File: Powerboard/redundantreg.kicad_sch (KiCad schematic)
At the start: 24 parts, among them Q10 MCH6351, Q9 MCH6351, U6 LM2679T-3.3-iclr, U7 LM2679T-3.3-iclr, U8 LTC4412xS6, U9 LTC4412xS6

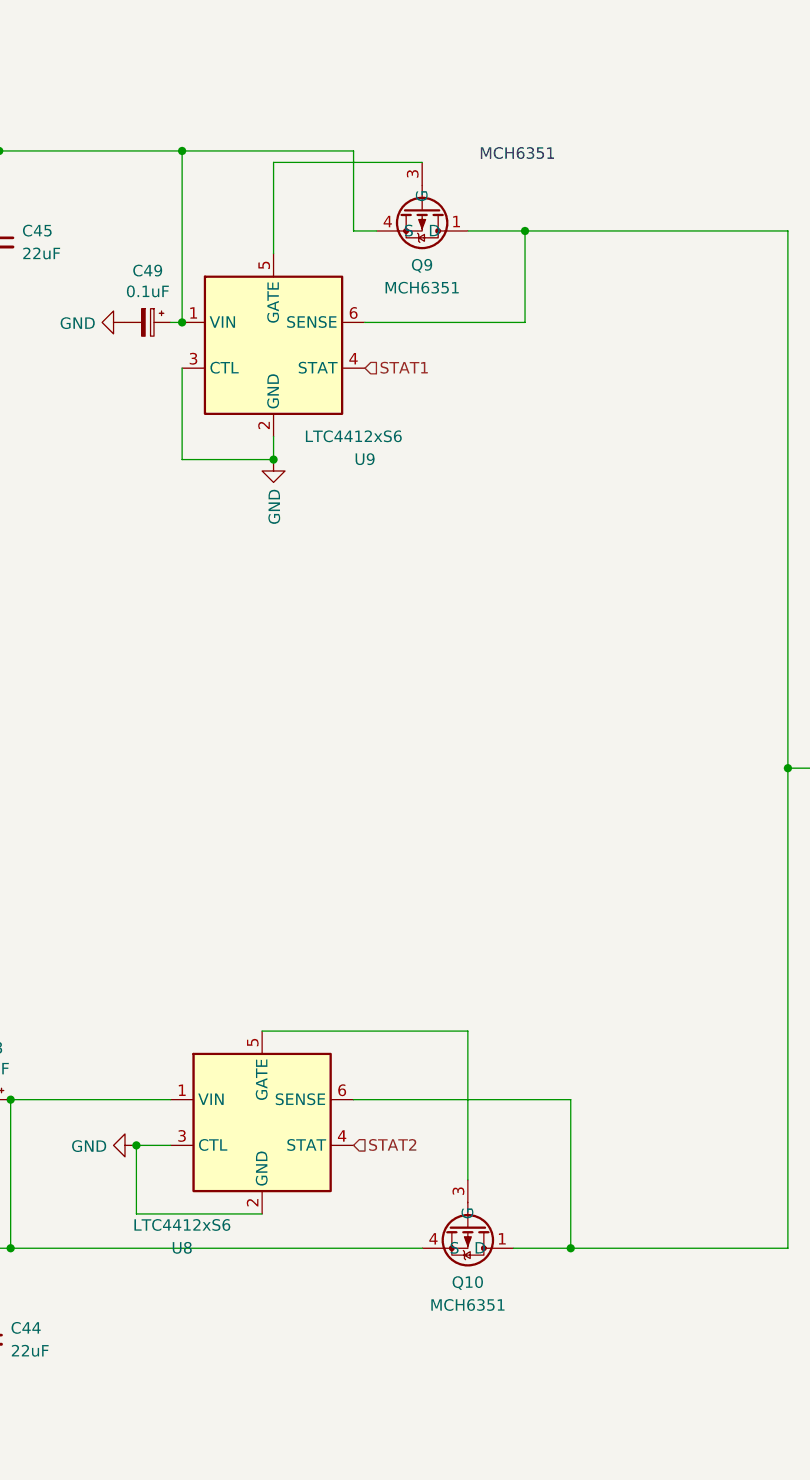
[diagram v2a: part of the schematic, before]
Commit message: swapping mosfets the right way around
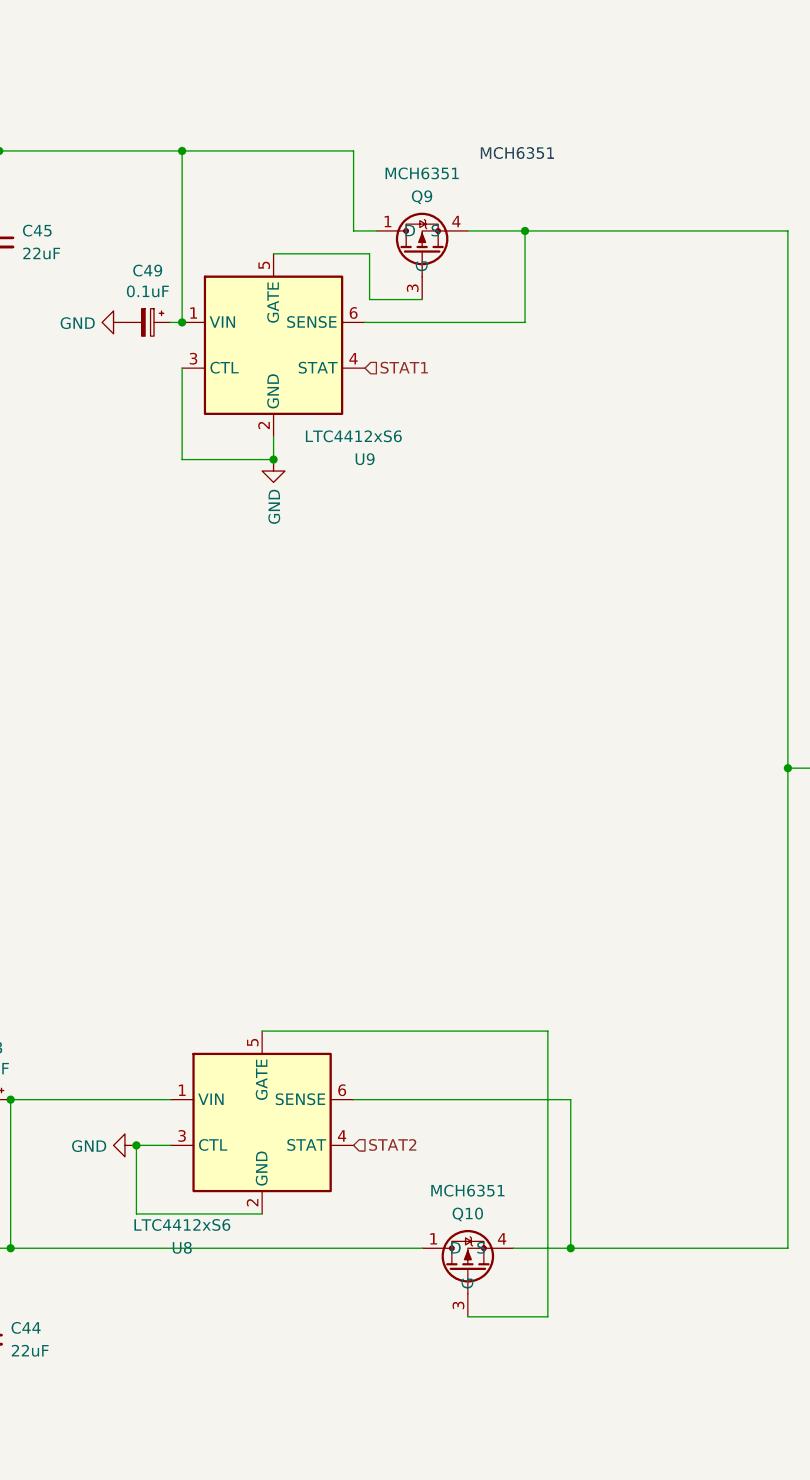
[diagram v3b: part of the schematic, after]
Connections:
- net Vout: now also Q10.4 (S), Q9.4 (S); no longer Q10.1 (D), Q10.2 (D), Q10.5 (D), Q10.6 (D), Q9.1 (D), Q9.2 (D), Q9.5 (D), Q9.6 (D)
- net at C38.1, C40.1, C44.1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: now also Q10.1 (D), Q10.2 (D), Q10.5 (D), Q10.6 (D); no longer Q10.4 (S)
- net at C39.1, C41.1, C45.1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: now also Q9.1 (D), Q9.2 (D), Q9.5 (D), Q9.6 (D); no longer Q9.4 (S)
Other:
- moved on the sheet: Q10, Q9
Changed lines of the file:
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@@
-    (stroke (width 0) (type default) (color 0 0 0 0))
-  )
-  (wire (pts (xy 200.66 26.67) (xy 200.66 36.83))
-    (stroke (width 0) (type default) (color 0 0 0 0))
-  )
-  (wire (pts (xy 200.66 26.67) (xy 217.17 26.67))
     (stroke (width 0) (type default) (color 0 0 0 0))
   )
@@
     (stroke (width 0) (type default) (color 0 0 0 0))
   )
+  (wire (pts (xy 200.66 36.83) (xy 211.328 36.83))
+    (stroke (width 0) (type default) (color 0 0 0 0))
+  )
   (wire (pts (xy 158.75 25.4) (xy 163.83 25.4))
     (stroke (width 0) (type default) (color 0 0 0 0))
@@
     (stroke (width 0) (type default) (color 0 0 0 0))
   )
+  (wire (pts (xy 231.14 154.94) (xy 222.25 154.94))
+    (stroke (width 0) (type default) (color 0 0 0 0))
+  )
   (wire (pts (xy 158.75 147.32) (xy 163.83 147.32))
     (stroke (width 0) (type default) (color 0 0 0 0))
@@
     (stroke (width 0) (type default) (color 0 0 0 0))
   )
-  (wire (pts (xy 222.25 123.19) (xy 222.25 139.7))
-    (stroke (width 0) (type default) (color 0 0 0 0))
-  )
   (wire (pts (xy 190.5 25.4) (xy 190.5 44.45))
     (stroke (width 0) (type default) (color 0 0 0 0))
@@
     (stroke (width 0) (type default) (color 0 0 0 0))
   )
-  (wire (pts (xy 199.39 123.19) (xy 222.25 123.19))
-    (stroke (width 0) (type default) (color 0 0 0 0))
-  )
   (wire (pts (xy 163.83 39.37) (xy 163.83 41.91))
     (stroke (width 0) (type default) (color 0 0 0 0))
@@
     (stroke (width 0) (type default) (color 0 0 0 0))
   )
+  (wire (pts (xy 199.39 123.19) (xy 231.14 123.19))
+    (stroke (width 0) (type default) (color 0 0 0 0))
+  )
   (wire (pts (xy 189.23 44.45) (xy 190.5 44.45))
     (stroke (width 0) (type default) (color 0 0 0 0))
@@
     (stroke (width 0) (type default) (color 0 0 0 0))
   )
+  (wire (pts (xy 231.14 123.19) (xy 231.14 154.94))
+    (stroke (width 0) (type default) (color 0 0 0 0))
+  )
   (wire (pts (xy 190.5 59.69) (xy 200.66 59.69))
     (stroke (width 0) (type default) (color 0 0 0 0))
@@
     (stroke (width 0) (type default) (color 0 0 0 0))
   )
+  (wire (pts (xy 211.328 36.83) (xy 211.328 41.91))
+    (stroke (width 0) (type default) (color 0 0 0 0))
+  )
   (wire (pts (xy 25.4 147.32) (xy 64.77 147.32))
     (stroke (width 0) (type default) (color 0 0 0 0))
@@
   )
   (wire (pts (xy 189.23 135.89) (xy 185.42 135.89))
+    (stroke (width 0) (type default) (color 0 0 0 0))
+  )
+  (wire (pts (xy 211.328 41.91) (xy 217.17 41.91))
     (stroke (width 0) (type default) (color 0 0 0 0))
   )
@@
     (pin "2")
   )
-  (symbol (lib_id "iclr:MCH6351") (at 236.22 22.86 270) (unit 1)
-    (in_bom yes) (on_board yes)
-    (property "Reference" "Q9" (id 0) (at 217.17 38.1 90))
-    (property "Value" "MCH6351" (id 1) (at 217.17 40.64 90))
-    (property "Footprint" "Package_TO_SOT_SMD:SOT-363_SC-70-6" (id 2) (at 218.44 38.1 0)
-      (effects (font (size 1.27 1.27)) hide)
-    )
-    (property "Datasheet" "" (id 3) (at 218.44 38.1 0)
+  (symbol (lib_id "iclr:MCH6351") (at 198.12 45.72 90) (unit 1)
+    (in_bom yes) (on_board yes)
+    (property "Reference" "Q9" (id 0) (at 217.17 30.48 90))
+    (property "Value" "MCH6351" (id 1) (at 217.17 27.94 90))
+    (property "Footprint" "Package_TO_SOT_SMD:SOT-363_SC-70-6" (id 2) (at 215.9 30.48 0)
+      (effects (font (size 1.27 1.27)) hide)
+    )
+    (property "Datasheet" "" (id 3) (at 215.9 30.48 0)
       (effects (font (size 1.27 1.27)) hide)
     )
@@
     (pin "2")
   )
-  (symbol (lib_id "iclr:MCH6351") (at 241.3 135.89 270) (unit 1)
-    (in_bom yes) (on_board yes)
-    (property "Reference" "Q10" (id 0) (at 222.25 151.13 90))
-    (property "Value" "MCH6351" (id 1) (at 222.25 153.67 90))
-    (property "Footprint" "Package_TO_SOT_SMD:SOT-363_SC-70-6" (id 2) (at 223.52 151.13 0)
-      (effects (font (size 1.27 1.27)) hide)
-    )
-    (property "Datasheet" "" (id 3) (at 223.52 151.13 0)
-      (effects (font (size 1.27 1.27)) hide)
-    )
+  (symbol (lib_id "iclr:MCH6351") (at 203.2 158.75 90) (unit 1)
+    (in_bom yes) (on_board yes)
+    (property "Reference" "Q10" (id 0) (at 222.25 143.51 90))
+    (property "Value" "MCH6351" (id 1) (at 222.25 140.97 90))
+    (property "Footprint" "Package_TO_SOT_SMD:SOT-363_SC-70-6" (id 2) (at 220.98 143.51 0)
+      (effects (font (size 1.27 1.27)) hide)
+    )
+    (property "Datasheet" "" (id 3) (at 220.98 143.51 0)
+      (effects (font (size 1.27 1.27)) hide)
+    )

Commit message: dan's review
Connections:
- net GND: now also U6.5 (CURRENT_ADJ), U7.5 (CURRENT_ADJ)
- no-connect marks 4 -> 2
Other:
- note added: "Wurth Elektronik 7447709150"
- note removed: "Wurth Elektronik 744770115"
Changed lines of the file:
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@@
   (junction (at 134.62 163.83) (diameter 0) (color 0 0 0 0)
   )
-  (no_connect (at 125.73 33.02))
   (no_connect (at 127 152.4))
-  (no_connect (at 127 154.94))
   (no_connect (at 125.73 30.48))
   (wire (pts (xy 163.83 147.32) (xy 163.83 153.67))
@@
     (stroke (width 0) (type default) (color 0 0 0 0))
   )
-  (text "Wurth Elektronik 744770115" (at 130.9662 18.4246 0)
+  (text "Wurth Elektronik 7447709150" (at 130.9662 18.4246 0)
     (effects (font (size 1.27 1.27)) (justify left bottom))
   )
@@
     (pin "6")
   )
+  (symbol (lib_id "power:GND") (at 127 154.94 0) (unit 1)
+    (in_bom yes) (on_board yes)
+    (property "Reference" "#PWR0179" (id 0) (at 127 161.29 0)
+      (effects (font (size 1.27 1.27)) hide)
+    )
+    (property "Value" "GND" (id 1) (at 127.127 158.1912 90)
+      (effects (font (size 1.27 1.27)) (justify right))
+    )
+    (property "Footprint" "" (id 2) (at 127 154.94 0)
+      (effects (font (size 1.27 1.27)) hide)
+    )
+    (property "Datasheet" "" (id 3) (at 127 154.94 0)
+      (effects (font (size 1.27 1.27)) hide)
+    )
+    (pin "1")
+  )
   (symbol (lib_id "Device:C_Small") (at 168.91 157.48 0) (unit 1)
     (in_bom yes) (on_board yes) (fields_autoplaced)
@@
     (pin "3")
   )
+  (symbol (lib_id "power:GND") (at 125.73 33.02 0) (unit 1)
+    (in_bom yes) (on_board yes)
+    (property "Reference" "#PWR0180" (id 0) (at 125.73 39.37 0)
+      (effects (font (size 1.27 1.27)) hide)
+    )
+    (property "Value" "GND" (id 1) (at 125.857 36.2712 90)
+      (effects (font (size 1.27 1.27)) (justify right))
+    )
+    (property "Footprint" "" (id 2) (at 125.73 33.02 0)
+      (effects (font (size 1.27 1.27)) hide)
+    )
+    (property "Datasheet" "" (id 3) (at 125.73 33.02 0)
+      (effects (font (size 1.27 1.27)) hide)
+    )
+    (pin "1")
+  )
   (symbol (lib_id "Device:C_Polarized") (at 158.75 35.56 0) (unit 1)
